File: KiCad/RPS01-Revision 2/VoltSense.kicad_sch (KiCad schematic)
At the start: 6 parts

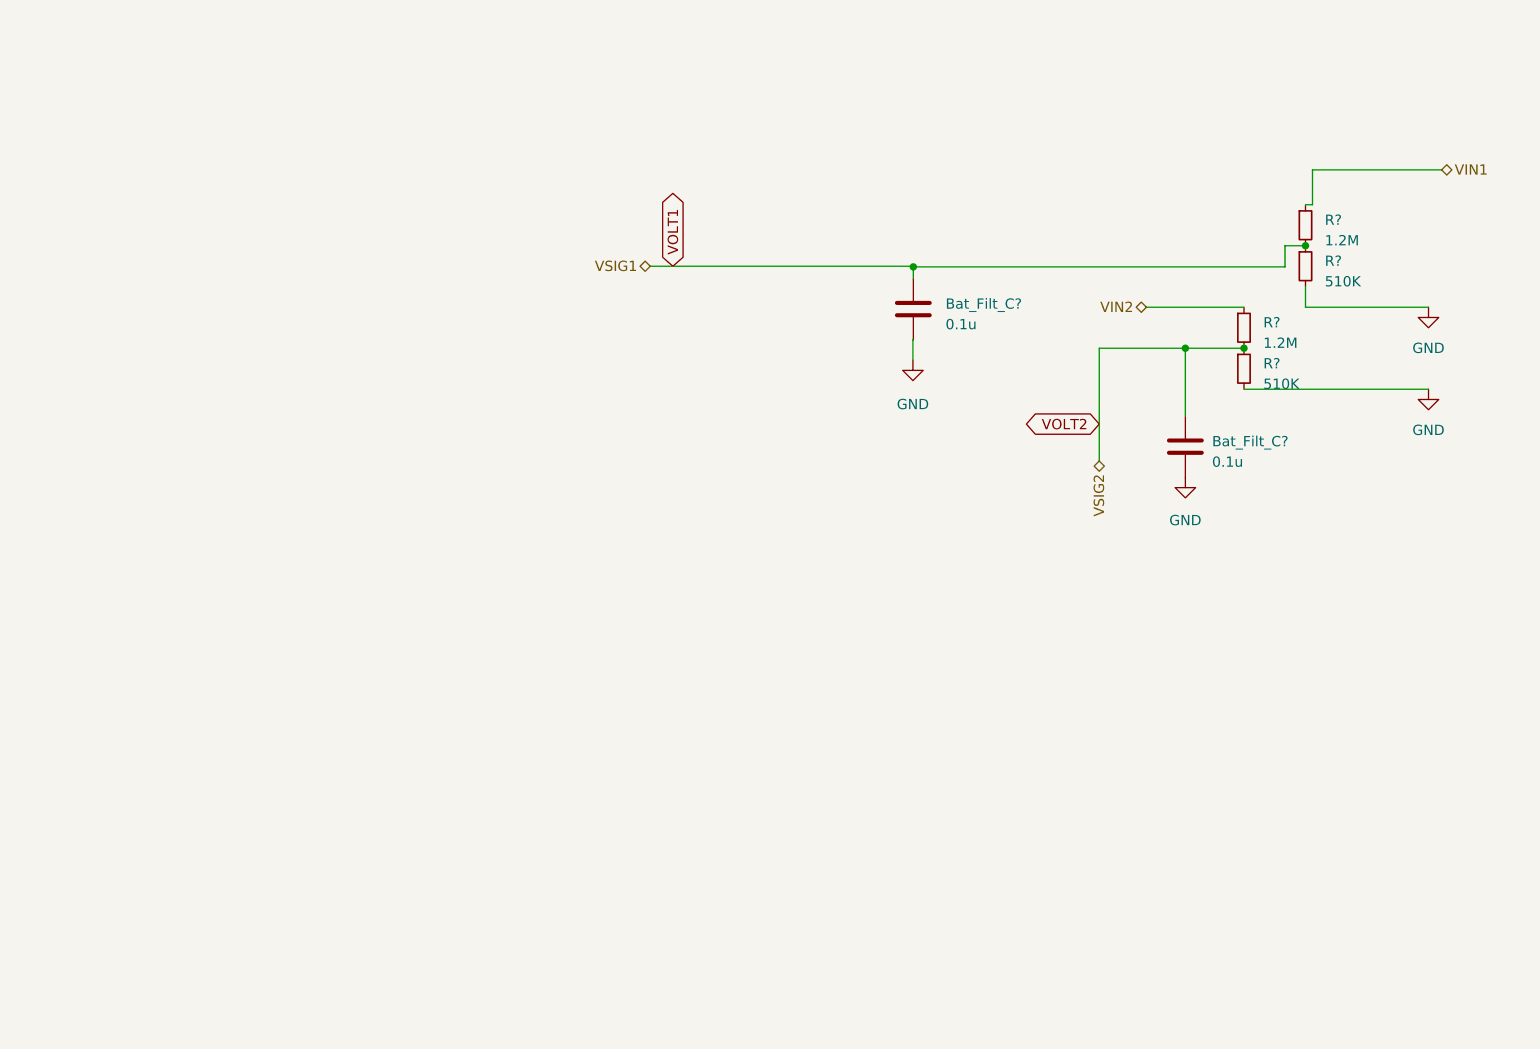
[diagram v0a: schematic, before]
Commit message: Updated Buffer, Precision LDO, new LDO
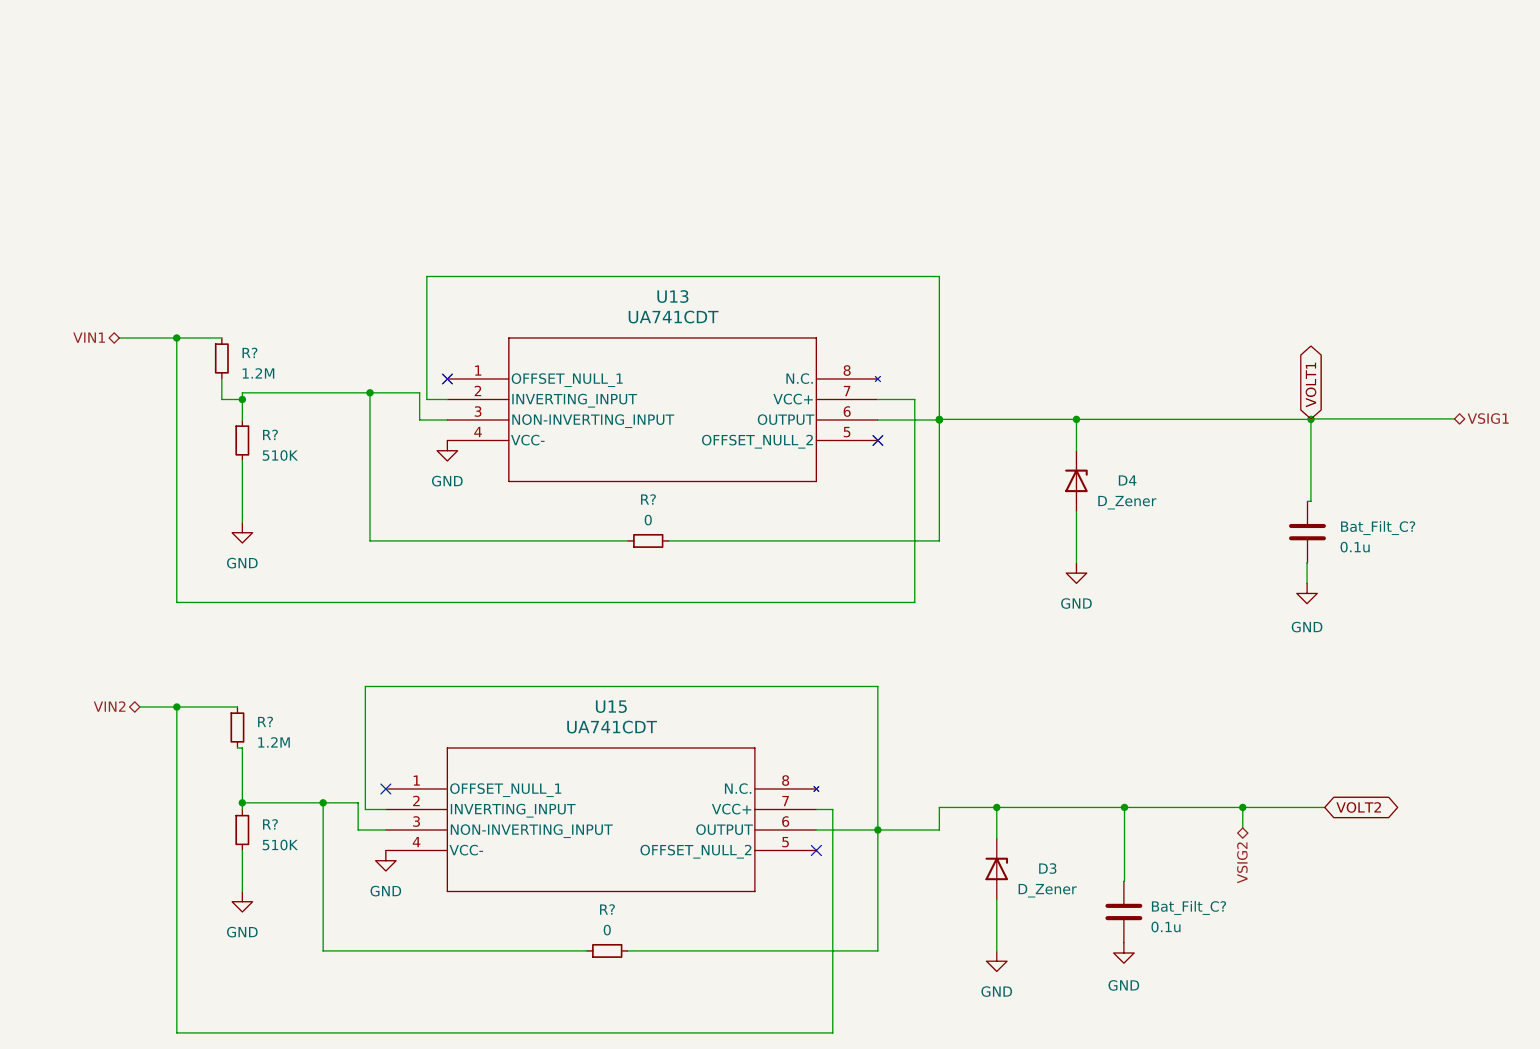
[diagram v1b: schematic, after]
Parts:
- added D3, D4: D_Zener, symbol Device:D_Zener
- added R? (x2): 0, Resistor_SMD:R_1206_3216Metric, symbol Device:R_Small
- added U13, U15: UA741CDT, Mechatronic Footprints:UA741CDT_D8_TEX_STM, symbol UA741CDT:UA741CDT
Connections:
- net GND: now also D3.2 (A), D4.2 (A), U13.4 (VCC-), U15.4 (VCC-)
- net VIN1: now also U13.7 (VCC+)
- net VIN2: now also U15.7 (VCC+)
- net VOLT1: now also D4.1 (K), R?.2, U13.2 (INVERTING_INPUT), U13.6 (OUTPUT); no longer R?.1, R?.2
- net VOLT2: now also D3.1 (K), R?.2, U15.2 (INVERTING_INPUT), U15.6 (OUTPUT); no longer R?.1, R?.2
- new net: R?.1, R?.1, R?.2, U13.3 (NON-INVERTING_INPUT)
- new net: R?.1, R?.1, R?.2, U15.3 (NON-INVERTING_INPUT)
- no-connect marks 0 -> 4
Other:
- moved on the sheet: Bat_Filt_C?, R?

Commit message: update volt sense diode refereneces
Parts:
- D3, D4: value D_Zener -> MMSZ5247BT1G; footprint (none) -> Diode_SMD:D_SOD-123
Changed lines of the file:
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@@
       (effects (font (size 1.27 1.27)) (justify left))
     )
-    (property "Value" "D_Zener" (at 147.32 127 90)
-      (effects (font (size 1.27 1.27)) (justify left))
-    )
-    (property "Footprint" "" (at 144.78 124.46 0)
-      (effects (font (size 1.27 1.27)) hide)
-    )
-    (property "Datasheet" "~" (at 144.78 124.46 0)
+    (property "Value" "MMSZ5247BT1G" (at 147.32 127 90)
+      (effects (font (size 1.27 1.27)) (justify left))
+    )
+    (property "Footprint" "Diode_SMD:D_SOD-123" (at 144.78 124.46 0)
+      (effects (font (size 1.27 1.27)) hide)
+    )
+    (property "Datasheet" "https://www.digikey.com/en/products/detail/onsemi/MMSZ5247BT1G/1749046" (at 144.78 124.46 0)
       (effects (font (size 1.27 1.27)) hide)
     )
@@
       (effects (font (size 1.27 1.27)) (justify left))
     )
-    (property "Value" "D_Zener" (at 157.1945 78.9181 90)
-      (effects (font (size 1.27 1.27)) (justify left))
-    )
-    (property "Footprint" "" (at 154.6545 76.3781 0)
-      (effects (font (size 1.27 1.27)) hide)
-    )
-    (property "Datasheet" "~" (at 154.6545 76.3781 0)
-      (effects (font (size 1.27 1.27)) hide)
-    )
+    (property "Value" "MMSZ5247BT1G" (at 157.1945 78.9181 90)
+      (effects (font (size 1.27 1.27)) (justify left))
+    )
+    (property "Footprint" "Diode_SMD:D_SOD-123" (at 154.6545 76.3781 0)
+      (effects (font (size 1.27 1.27)) hide)
+    )
+    (property "Datasheet" "https://www.digikey.com/en/products/detail/onsemi/MMSZ5247BT1G/1749046" (at 154.6545 76.3781 0)
+      (effects (font (size 1.27 1.27)) hide)
+    )

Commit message: update led resistor and voltsense references
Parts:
- renumbered D4 to D1_VSENSE, D3 to D2_VSENSE
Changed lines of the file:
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@@
   (symbol (lib_id "Device:R_Small") (at 51.308 71.374 0) (unit 1)
     (in_bom yes) (on_board yes) (dnp no) (fields_autoplaced)
-    (property "Reference" "R?" (at 53.6956 70.739 0)
-      (effects (font (size 1.27 1.27)) (justify left))
-    )
-    (property "Value" "510K" (at 53.6956 73.279 0)
+    (property "Reference" "R?" (at 53.34 70.739 0)
+      (effects (font (size 1.27 1.27)) (justify left))
+    )
+    (property "Value" "510K" (at 53.34 73.279 0)
       (effects (font (size 1.27 1.27)) (justify left))
     )
@@
         )
         (path "/14930f15-c0a0-4b55-93e6-b112548415f6/86aa0a4b-8e23-451d-9b8a-c1446d1d5d38"
-          (reference "R_P8") (unit 1)
+          (reference "R2_VSENSE") (unit 1)
         )
       )
@@
   (symbol (lib_id "Device:D_Zener") (at 144.78 124.46 270) (unit 1)
     (in_bom yes) (on_board yes) (dnp no)
-    (property "Reference" "D3" (at 149.86 124.46 90)
+    (property "Reference" "D2_VSENSE" (at 149.86 124.46 90)
       (effects (font (size 1.27 1.27)) (justify left))
     )
@@
       (project "rps01"
         (path "/14930f15-c0a0-4b55-93e6-b112548415f6/86aa0a4b-8e23-451d-9b8a-c1446d1d5d38"
-          (reference "D3") (unit 1)
+          (reference "D2_VSENSE") (unit 1)
         )
       )
@@
         )
         (path "/14930f15-c0a0-4b55-93e6-b112548415f6/86aa0a4b-8e23-451d-9b8a-c1446d1d5d38"
-          (reference "R_V1_Buf_Enable1") (unit 1)
+          (reference "REN1_VSENSE") (unit 1)
         )
       )
@@
   (symbol (lib_id "Device:R_Small") (at 50.6984 106.934 0) (unit 1)
     (in_bom yes) (on_board yes) (dnp no) (fields_autoplaced)
-    (property "Reference" "R?" (at 53.086 106.299 0)
-      (effects (font (size 1.27 1.27)) (justify left))
-    )
-    (property "Value" "1.2M" (at 53.086 108.839 0)
+    (property "Reference" "R?" (at 53.34 106.299 0)
+      (effects (font (size 1.27 1.27)) (justify left))
+    )
+    (property "Value" "1.2M" (at 53.34 108.839 0)
       (effects (font (size 1.27 1.27)) (justify left))
     )
@@
         )
         (path "/14930f15-c0a0-4b55-93e6-b112548415f6/86aa0a4b-8e23-451d-9b8a-c1446d1d5d38"
-          (reference "R_P9") (unit 1)
+          (reference "R3_VSENSE") (unit 1)
         )
       )
@@
         )
         (path "/14930f15-c0a0-4b55-93e6-b112548415f6/86aa0a4b-8e23-451d-9b8a-c1446d1d5d38"
-          (reference "R_V2_Buf_Enable1") (unit 1)
+          (reference "REN2_VSENSE") (unit 1)
         )
       )
@@
   (symbol (lib_id "Device:D_Zener") (at 154.6545 76.3781 270) (unit 1)
     (in_bom yes) (on_board yes) (dnp no)
-    (property "Reference" "D4" (at 159.7345 76.3781 90)
+    (property "Reference" "D1_VSENSE" (at 159.7345 76.3781 90)
       (effects (font (size 1.27 1.27)) (justify left))
     )
@@
       (project "rps01"
         (path "/14930f15-c0a0-4b55-93e6-b112548415f6/86aa0a4b-8e23-451d-9b8a-c1446d1d5d38"
-          (reference "D4") (unit 1)
+          (reference "D1_VSENSE") (unit 1)
         )
       )
@@
         )
         (path "/14930f15-c0a0-4b55-93e6-b112548415f6/86aa0a4b-8e23-451d-9b8a-c1446d1d5d38"
-          (reference "C21") (unit 1)
+          (reference "CF2_VSENSE") (unit 1)
         )
       )
@@
   (symbol (lib_id "Device:C") (at 183.2771 82.7281 0) (unit 1)
     (in_bom yes) (on_board yes) (dnp no) (fields_autoplaced)
-    (property "Reference" "Bat_Filt_C?" (at 187.2649 82.0931 0)
-      (effects (font (size 1.27 1.27)) (justify left))
-    )
-    (property "Value" "0.1u" (at 187.2649 84.6331 0)
+    (property "Reference" "Bat_Filt_C?" (at 186.69 82.0931 0)
+      (effects (font (size 1.27 1.27)) (justify left))
+    )
+    (property "Value" "0.1u" (at 186.69 84.6331 0)
       (effects (font (size 1.27 1.27)) (justify left))
     )
@@
         )
         (path "/14930f15-c0a0-4b55-93e6-b112548415f6/86aa0a4b-8e23-451d-9b8a-c1446d1d5d38"
-          (reference "C20") (unit 1)
+          (reference "CF1_VSENSE") (unit 1)
         )
       )
@@
   (symbol (lib_id "Device:R_Small") (at 48.768 61.214 0) (unit 1)
     (in_bom yes) (on_board yes) (dnp no) (fields_autoplaced)
-    (property "Reference" "R?" (at 51.1556 60.579 0)
-      (effects (font (size 1.27 1.27)) (justify left))
-    )
-    (property "Value" "1.2M" (at 51.1556 63.119 0)
+    (property "Reference" "R?" (at 50.8 60.579 0)
+      (effects (font (size 1.27 1.27)) (justify left))
+    )
+    (property "Value" "1.2M" (at 50.8 63.119 0)
       (effects (font (size 1.27 1.27)) (justify left))
     )
@@
         )
         (path "/14930f15-c0a0-4b55-93e6-b112548415f6/86aa0a4b-8e23-451d-9b8a-c1446d1d5d38"
-          (reference "R_P7") (unit 1)
+          (reference "R1_VSENSE") (unit 1)
         )
       )
@@
   (symbol (lib_id "Device:R_Small") (at 51.308 119.634 0) (unit 1)
     (in_bom yes) (on_board yes) (dnp no) (fields_autoplaced)
-    (property "Reference" "R?" (at 53.6956 118.999 0)
-      (effects (font (size 1.27 1.27)) (justify left))
-    )
-    (property "Value" "510K" (at 53.6956 121.539 0)
+    (property "Reference" "R?" (at 53.34 118.999 0)
+      (effects (font (size 1.27 1.27)) (justify left))
+    )
+    (property "Value" "510K" (at 53.34 121.539 0)
       (effects (font (size 1.27 1.27)) (justify left))
     )
@@
         )
         (path "/14930f15-c0a0-4b55-93e6-b112548415f6/86aa0a4b-8e23-451d-9b8a-c1446d1d5d38"
-          (reference "R_P10") (unit 1)
-        )
-      )
+          (reference "R4_VSENSE") (unit 1)
+        )
+      )

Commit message: Button Footprints
Changed button footprints
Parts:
- renumbered D1_VSENSE to D1_VSENSE1, D2_VSENSE to D2_VSENSE1
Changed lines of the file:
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@@
         )
         (path "/14930f15-c0a0-4b55-93e6-b112548415f6/86aa0a4b-8e23-451d-9b8a-c1446d1d5d38"
-          (reference "R2_VSENSE") (unit 1)
+          (reference "R2_VSENSE1") (unit 1)
         )
       )
@@
   (symbol (lib_id "Device:D_Zener") (at 144.78 124.46 270) (unit 1)
     (in_bom yes) (on_board yes) (dnp no)
-    (property "Reference" "D2_VSENSE" (at 149.86 124.46 90)
+    (property "Reference" "D2_VSENSE1" (at 149.86 124.46 90)
       (effects (font (size 1.27 1.27)) (justify left))
     )
@@
       (project "rps01"
         (path "/14930f15-c0a0-4b55-93e6-b112548415f6/86aa0a4b-8e23-451d-9b8a-c1446d1d5d38"
-          (reference "D2_VSENSE") (unit 1)
+          (reference "D2_VSENSE1") (unit 1)
         )
       )
@@
         )
         (path "/14930f15-c0a0-4b55-93e6-b112548415f6/86aa0a4b-8e23-451d-9b8a-c1446d1d5d38"
-          (reference "REN1_VSENSE") (unit 1)
+          (reference "REN1_VSENSE1") (unit 1)
         )
       )
@@
         )
         (path "/14930f15-c0a0-4b55-93e6-b112548415f6/86aa0a4b-8e23-451d-9b8a-c1446d1d5d38"
-          (reference "R3_VSENSE") (unit 1)
+          (reference "R3_VSENSE1") (unit 1)
         )
       )
@@
         )
         (path "/14930f15-c0a0-4b55-93e6-b112548415f6/86aa0a4b-8e23-451d-9b8a-c1446d1d5d38"
-          (reference "REN2_VSENSE") (unit 1)
+          (reference "REN2_VSENSE1") (unit 1)
         )
       )
@@
   (symbol (lib_id "Device:D_Zener") (at 154.6545 76.3781 270) (unit 1)
     (in_bom yes) (on_board yes) (dnp no)
-    (property "Reference" "D1_VSENSE" (at 159.7345 76.3781 90)
+    (property "Reference" "D1_VSENSE1" (at 159.7345 76.3781 90)
       (effects (font (size 1.27 1.27)) (justify left))
     )
@@
       (project "rps01"
         (path "/14930f15-c0a0-4b55-93e6-b112548415f6/86aa0a4b-8e23-451d-9b8a-c1446d1d5d38"
-          (reference "D1_VSENSE") (unit 1)
+          (reference "D1_VSENSE1") (unit 1)
         )
       )
@@
         )
         (path "/14930f15-c0a0-4b55-93e6-b112548415f6/86aa0a4b-8e23-451d-9b8a-c1446d1d5d38"
-          (reference "CF2_VSENSE") (unit 1)
+          (reference "CF2_VSENSE1") (unit 1)
         )
       )
@@
         )
         (path "/14930f15-c0a0-4b55-93e6-b112548415f6/86aa0a4b-8e23-451d-9b8a-c1446d1d5d38"
-          (reference "CF1_VSENSE") (unit 1)
+          (reference "CF1_VSENSE1") (unit 1)
         )
       )
@@
         )
         (path "/14930f15-c0a0-4b55-93e6-b112548415f6/86aa0a4b-8e23-451d-9b8a-c1446d1d5d38"
-          (reference "R1_VSENSE") (unit 1)
+          (reference "R1_VSENSE1") (unit 1)
         )
       )
@@
         )
         (path "/14930f15-c0a0-4b55-93e6-b112548415f6/86aa0a4b-8e23-451d-9b8a-c1446d1d5d38"
-          (reference "R4_VSENSE") (unit 1)
-        )
-      )
+          (reference "R4_VSENSE1") (unit 1)
+        )
+      )

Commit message: updates
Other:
- moved on the sheet: Bat_Filt_C?, D1_VSENSE1, D2_VSENSE1, R?, U13, U15

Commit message: Only Switches left
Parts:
- R? (x2): footprint Resistor_SMD:R_1206_3216Metric -> Resistor_SMD:R_0603_1608Metric_Pad0.98x0.95mm_HandSolder
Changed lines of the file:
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@@
       (effects (font (size 1.27 1.27)))
     )
-    (property "Footprint" "Resistor_SMD:R_1206_3216Metric" (at 96.012 51.562 0)
+    (property "Footprint" "Resistor_SMD:R_0603_1608Metric_Pad0.98x0.95mm_HandSolder" (at 96.012 51.562 0)
       (effects (font (size 1.27 1.27)) hide)
     )
@@
       (effects (font (size 1.27 1.27)))
     )
-    (property "Footprint" "Resistor_SMD:R_1206_3216Metric" (at 90.932 102.362 0)
+    (property "Footprint" "Resistor_SMD:R_0603_1608Metric_Pad0.98x0.95mm_HandSolder" (at 90.932 102.362 0)
       (effects (font (size 1.27 1.27)) hide)
     )
